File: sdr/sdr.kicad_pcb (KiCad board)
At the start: 6 copper layers, 85 x 53 mm, 97 parts, among them J1 USB_C_Receptacle_USB2.0, J2 Conn_01x06, J3 Conn_Coaxial, J4 AudioJack4, Q5 AO3400A, Q6 AO3401A, SW1 RESET, SW2 KEY, SW3 PTT, U1 AMS1117-3.3, U10 BGA2817, U11 74LVC1G66, U12 74LVC1G66, U13 74LVC1G66, U14 74LVC1G66, U2 MS5351M, U3 LM4871M/TR_C383075, U4 CH32V305RBT6, U5 BGA2817, U7 74LVC1G66, U8 FM1630C, U9 AD8001AR, Y1 25MHz, Y2 25MHz

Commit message: First version 0.1 completed
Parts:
- removed U9: AD8001AR, Package_SO:SOIC-8_3.9x4.9mm_P1.27mm
- added J5: Screen, Connector_PinSocket_2.54mm:PinSocket_1x04_P2.54mm_Vertical, F.Cu at (158.6, 84.8)
- added U6: GS8091-TR, Package_TO_SOT_SMD:SOT-23-5, F.Cu at (184.9, 95.8)
- C19, C20: value 2p -> 2.2p
- C4: value 390n -> 330n
- J4: value AudioJack4 -> PJ-320D
- R23, R29: value 4.7 -> 10
- moved C21 15.3 mm to (192.2, 95.8)
- moved R32 11.3 mm to (190.5, 94.8), turned to 0 degrees
- moved C25 10.5 mm to (179.8, 95.8)
- moved R27 10.5 mm to (181.0, 95.7)
- moved R31 8.85 mm to (181.0, 98.5), turned to 180 degrees
- moved C26 8.29 mm to (189.0, 95.2), turned to -90 degrees
- moved C27 6.25 mm to (188.0, 95.2)
- moved R30 5.12 mm to (183.2, 98.5), turned to 180 degrees
- moved R24 3.40 mm to (186.0, 99.5)
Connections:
- U4 pad 29: unconnected-(U4-PB10-Pad29) -> OLED_SCL
- U4 pad 30: unconnected-(U4-PB11-Pad30) -> OLED_SDA
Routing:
- net OLED_SDA: track 0.00 -> 45.5 mm, vias 0 -> 1
- net OLED_SCL: track 0.00 -> 43.0 mm, vias 0 -> 1
- net +5P: track 18.9 -> 10.8 mm
- net /TX Amplifier/RF_IN: track 22.7 -> 27.6 mm
- net V_BIAS: track 12.2 -> 7.98 mm
- net Net-(U6--): track 3.54 -> 2.31 mm
- net +5V: track 15.9 -> 15.2 mm
- net /CPU/ADC_I: track 84.1 -> 84.4 mm, vias 3 -> 5
- net GND: vias 146 -> 247
- net /Freq Synthesizer/LO_I: vias 3 -> 5
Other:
- board text added: "{dblquote}el Cheapo{dblquote} SDR v0.1 May 2023 Tim Molteno"
- board text removed: "SDR 0.1 Tim Molteno"

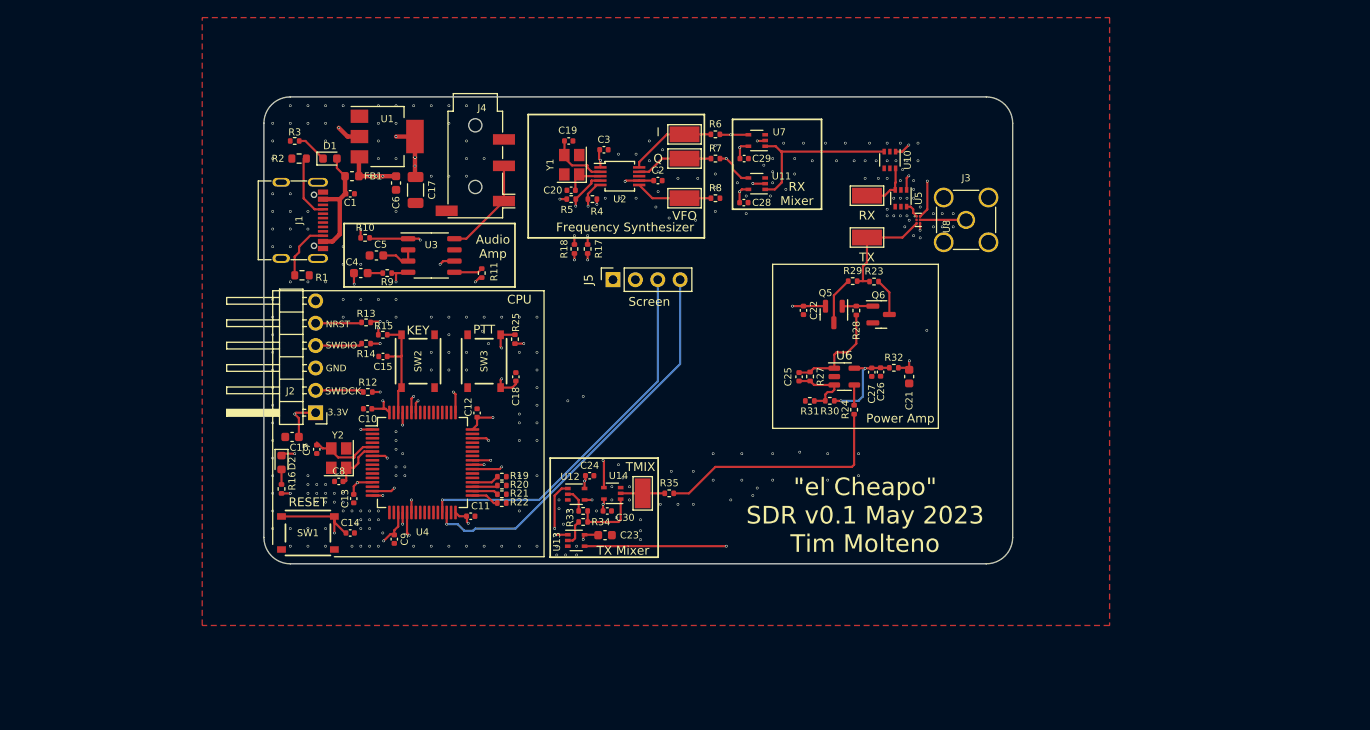
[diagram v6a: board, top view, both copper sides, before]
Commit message: Update the via size. Reduce footprints outside board.
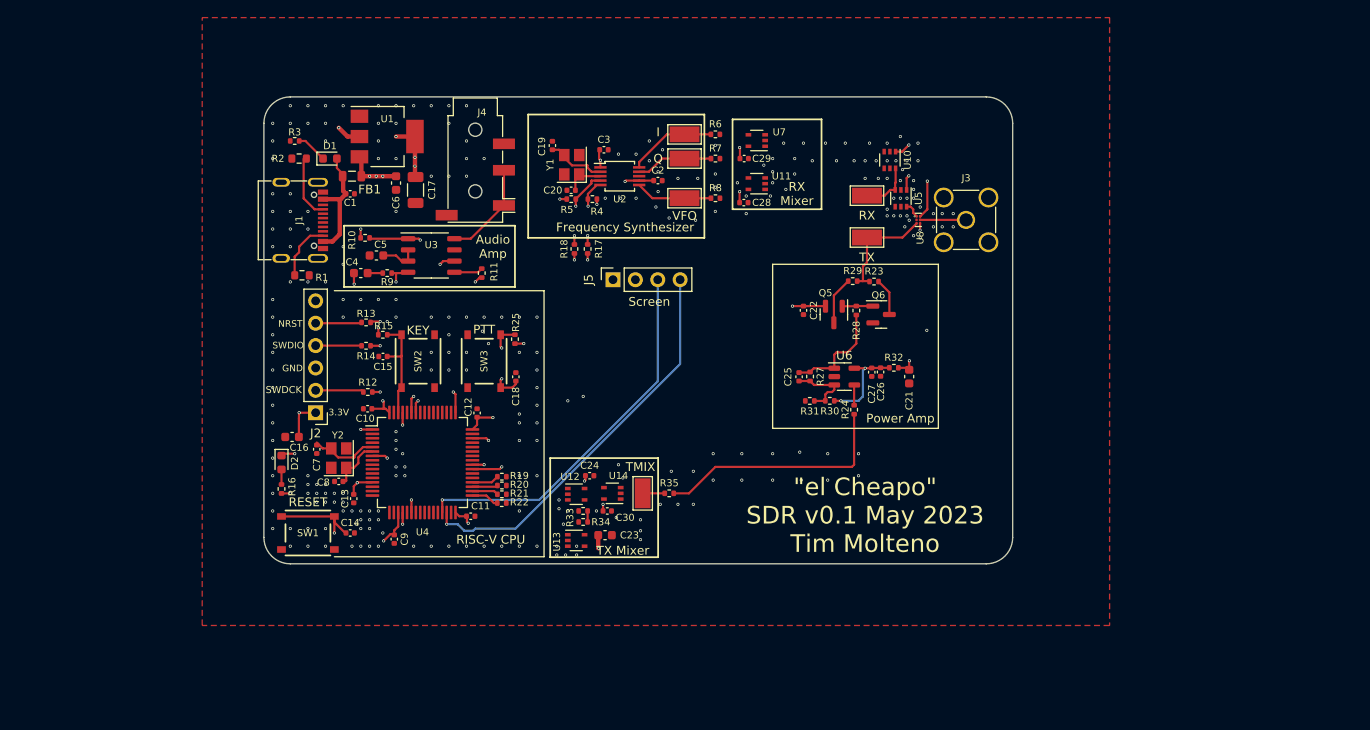
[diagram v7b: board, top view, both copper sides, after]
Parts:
- FB1: value BLM18KG221SN1D -> GZ2012D101TF; footprint Inductor_SMD:L_0603_1608Metric -> Inductor_SMD:L_0805_2012Metric
- J2: footprint Connector_PinHeader_2.54mm:PinHeader_1x06_P2.54mm_Horizontal -> Connector_PinHeader_2.54mm:PinHeader_1x06_P2.54mm_Vertical
- moved C19 1.92 mm to (151.8, 69.5), turned to -90 degrees
- moved J4 0.50 mm to (143.0, 72.5)
- moved R14 0.25 mm to (130.6, 92.2)
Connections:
- R33 pad 1: Net-(R33-Pad1) -> unconnected-(R33-Pad1)
- R34 pad 2: Net-(R34-Pad2) -> unconnected-(R34-Pad2)
- U11 pad 1: /Mixer I/RF -> unconnected-(U11-Pad1)
- U11 pad 2: /CPU/ADC_Q -> unconnected-(U11-Pad2)
- U11 pad 3: GND -> (no net)
- U11 pad 4: /Freq Synthesizer/LO_Q -> unconnected-(U11-Pad4)
- U11 pad 5: +3.3V -> (no net)
- U12 pad 1: /Audio Output/AUDIO -> unconnected-(U12-Pad1)
- U12 pad 2: Net-(R33-Pad1) -> unconnected-(U12-Pad2)
- U12 pad 3: GND -> (no net)
- U12 pad 4: /Freq Synthesizer/LO_I -> unconnected-(U12-Pad4)
- U12 pad 5: +3.3V -> (no net)
- U13 pad 1: /CPU/DAC_Q -> unconnected-(U13-Pad1)
- U13 pad 2: Net-(R34-Pad2) -> unconnected-(U13-Pad2)
- U13 pad 3: GND -> (no net)
- U13 pad 4: /Freq Synthesizer/LO_Q -> unconnected-(U13-Pad4)
- U13 pad 5: +3.3V -> (no net)
- U14 pad 1: Net-(R33-Pad2) -> unconnected-(U14-Pad1)
- U14 pad 2: /Tx Mixers/RF_OUT -> unconnected-(U14-Pad2)
- U14 pad 3: GND -> (no net)
- U14 pad 4: TXMIX_EN -> unconnected-(U14-Pad4)
- U14 pad 5: +3.3V -> (no net)
- U7 pad 1: /Mixer I/RF -> unconnected-(U7-Pad1)
- U7 pad 2: /CPU/ADC_I -> unconnected-(U7-Pad2)
- U7 pad 3: GND -> (no net)
- U7 pad 4: /Freq Synthesizer/LO_I -> unconnected-(U7-Pad4)
- U7 pad 5: +3.3V -> (no net)
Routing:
- net /CPU/ADC_I: track 84.4 -> 0.00 mm, vias 5 -> 0
- net /CPU/ADC_Q: track 80.0 -> 0.00 mm, vias 3 -> 0
- net /Freq Synthesizer/LO_Q: track 64.5 -> 0.00 mm, vias 2 -> 0
- net /Freq Synthesizer/LO_I: track 61.3 -> 0.00 mm, vias 5 -> 0
- net /Audio Output/AUDIO: track 58.4 -> 35.4 mm, vias 4 -> 3
- net /CPU/DAC_Q: track 20.7 -> 0.00 mm, vias 2 -> 0
- net /Mixer I/RF: track 19.5 -> 0.00 mm
- net TXMIX_EN: track 18.0 -> 0.00 mm, vias 2 -> 0
- net Net-(R33-Pad2): track 7.45 -> 1.25 mm
- net +3.3V: track 55.6 -> 50.5 mm, vias 27 -> 26
- net Net-(R34-Pad2): track 2.95 -> 0.00 mm
- net Net-(R33-Pad1): track 2.75 -> 0.00 mm
- net /Tx Mixers/RF_OUT: track 5.00 -> 2.50 mm
- net Net-(U2-CLK2): track 9.48 -> 8.77 mm
- net +5V: track 15.2 -> 15.1 mm, vias 8 -> 7
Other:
- board text added: "RISC-V CPU"
- board text removed: "CPU"

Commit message: Convert to a 4-layer board.
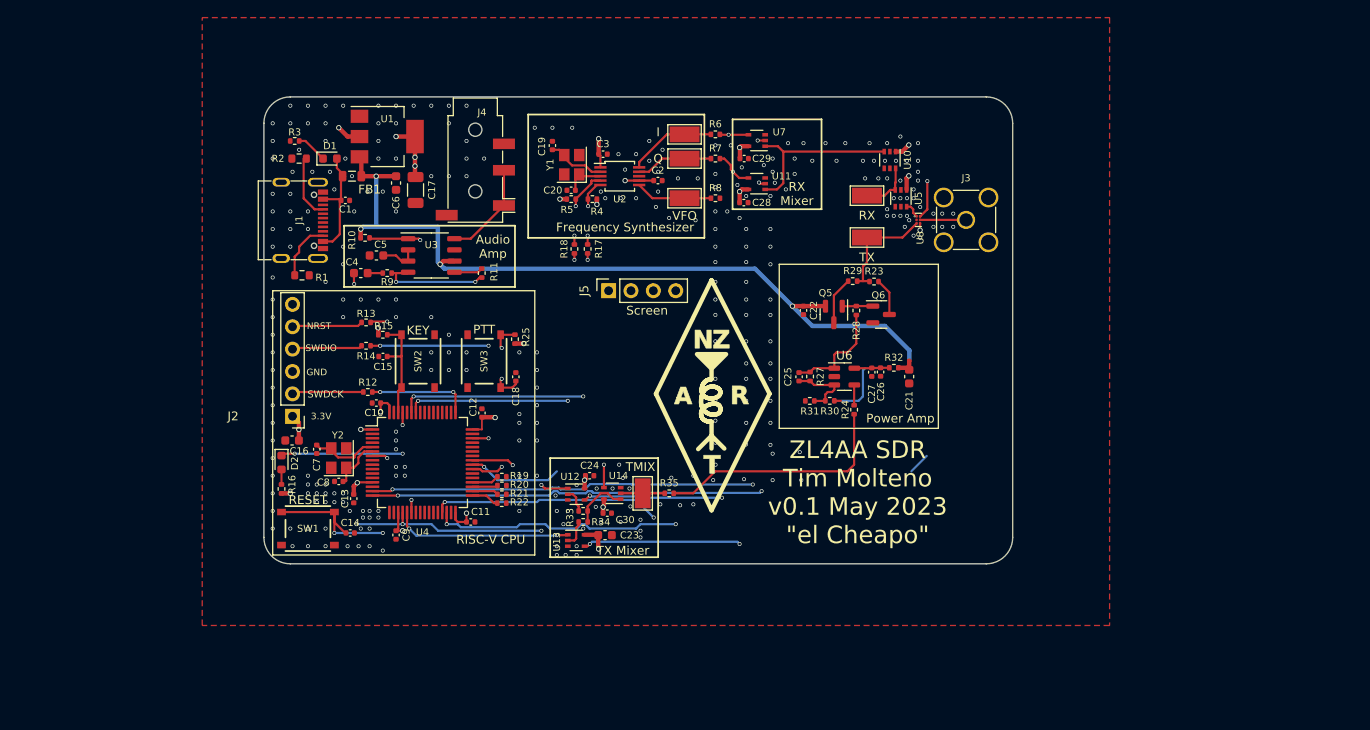
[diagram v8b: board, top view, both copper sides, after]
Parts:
- U3: value LM4871M/TR_C383075 -> LM4871M/TR
- moved J2 2.66 mm to (122.2, 100.2)
- moved J5 1.35 mm to (158.1, 86.0)
- moved C10 1.19 mm to (131.8, 98.8)
- moved C1 0.93 mm to (128.2, 75.8)
- moved C11 0.65 mm to (142.5, 112.2)
- moved C12 0.55 mm to (143.8, 99.9)
- moved C9 0.51 mm to (134.0, 113.7)
- moved C3 0.51 mm to (157.5, 70.5)
- moved SW1 0.50 mm to (124.0, 113.0)
- moved C16 0.40 mm to (122.2, 103.0)
- moved C30 0.25 mm to (158.0, 111.2)
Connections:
- R33 pad 1: unconnected-(R33-Pad1) -> Net-(R33-Pad1)
- R34 pad 2: unconnected-(R34-Pad2) -> Net-(R34-Pad2)
- U11 pad 1: unconnected-(U11-Pad1) -> /Mixer I/RF
- U11 pad 2: unconnected-(U11-Pad2) -> /CPU/ADC_Q
- U11 pad 3: (no net) -> GND
- U11 pad 4: unconnected-(U11-Pad4) -> /Freq Synthesizer/LO_Q
- U11 pad 5: (no net) -> +3.3V
- U12 pad 1: unconnected-(U12-Pad1) -> /Audio Output/AUDIO
- U12 pad 2: unconnected-(U12-Pad2) -> Net-(R33-Pad1)
- U12 pad 3: (no net) -> GND
- U12 pad 4: unconnected-(U12-Pad4) -> /Freq Synthesizer/LO_I
- U12 pad 5: (no net) -> +3.3V
- U13 pad 1: unconnected-(U13-Pad1) -> /CPU/DAC_Q
- U13 pad 2: unconnected-(U13-Pad2) -> Net-(R34-Pad2)
- U13 pad 3: (no net) -> GND
- U13 pad 4: unconnected-(U13-Pad4) -> /Freq Synthesizer/LO_Q
- U13 pad 5: (no net) -> +3.3V
- U14 pad 1: unconnected-(U14-Pad1) -> Net-(R33-Pad2)
- U14 pad 2: unconnected-(U14-Pad2) -> /Tx Mixers/RF_OUT
- U14 pad 3: (no net) -> GND
- U14 pad 4: unconnected-(U14-Pad4) -> TXMIX_EN
- U14 pad 5: (no net) -> +3.3V
- U7 pad 1: unconnected-(U7-Pad1) -> /Mixer I/RF
- U7 pad 2: unconnected-(U7-Pad2) -> /CPU/ADC_I
- U7 pad 3: (no net) -> GND
- U7 pad 4: unconnected-(U7-Pad4) -> /Freq Synthesizer/LO_I
- U7 pad 5: (no net) -> +3.3V
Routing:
- net /CPU/ADC_I: track 0.00 -> 83.8 mm, vias 0 -> 3
- net /CPU/ADC_Q: track 0.00 -> 80.6 mm, vias 0 -> 3
- net +5V: track 15.1 -> 92.6 mm, vias 7 -> 4
- net /Freq Synthesizer/LO_Q: track 0.00 -> 64.9 mm, vias 0 -> 3
- net /Freq Synthesizer/LO_I: track 0.00 -> 60.7 mm, vias 0 -> 3
- net RX_EN: track 88.3 -> 48.8 mm, vias 4 -> 2
- net /Audio Output/AUDIO: track 35.4 -> 59.8 mm, vias 3 -> 5
- net /CPU/DAC_Q: track 0.00 -> 20.3 mm, vias 0 -> 2
- net /Mixer I/RF: track 0.00 -> 19.7 mm
- net TXMIX_EN: track 0.00 -> 17.8 mm, vias 0 -> 2
- net OLED_SDA: track 45.5 -> 54.9 mm, vias 1 -> 2
- net OLED_SCL: track 43.0 -> 51.7 mm, vias 1 -> 2
- net +3.3V: track 50.5 -> 56.1 mm
- net Net-(R33-Pad2): track 1.25 -> 6.41 mm
- net Net-(R34-Pad2): track 0.00 -> 3.05 mm
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- removed copper zone on In4.Cu, net +5V
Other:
- copper layers 6 -> 4
- board text added: "ZL4AA SDR Tim Molteno v0.1 May 2023 {dblquote}el Cheapo{dblquote}"
- board text added: "ZL4AA Software Defined Radio 2.5 kHz -> 200 MHz Tim Molteno ZL4TCM tim@molteno.net v0.1, May 2023 https://github.com/tmolteno/zl4aa"
- board text removed: "{dblquote}el Cheapo{dblquote} SDR v0.1 May 2023 Tim Molteno"
